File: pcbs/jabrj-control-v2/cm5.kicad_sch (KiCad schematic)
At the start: 26 parts, among them J701 FFC3A20-05-G, J702 JST-SH-4-Vertical, Q701 DMN21D2UFB-7B, SW701 TS20-42-25-WT-160-SMT-TR, U701 PESD4USB3BTTS-QX, U702 NX3DV221GM

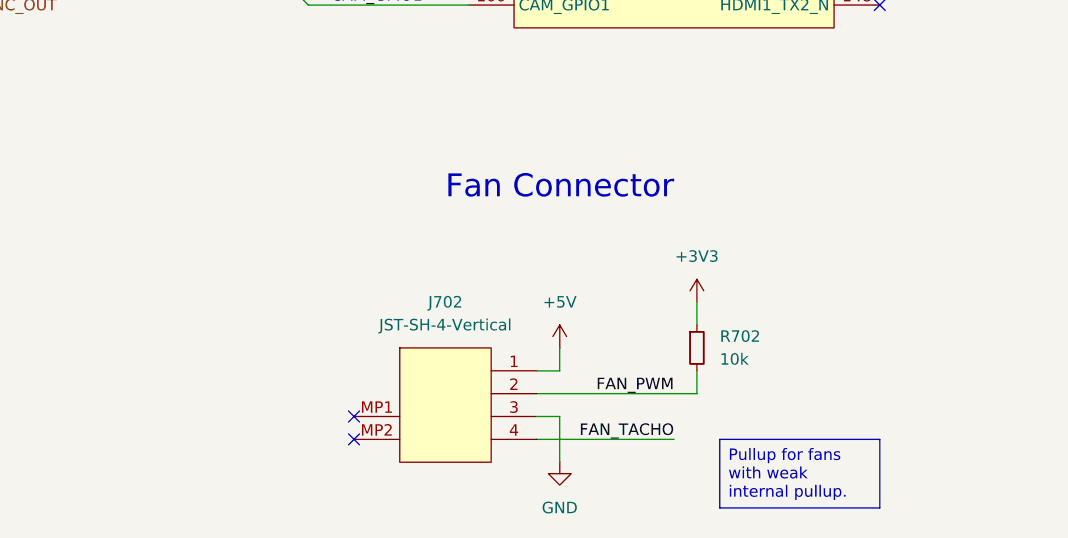
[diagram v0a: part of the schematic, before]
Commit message: Fixed 5V buck inductor value
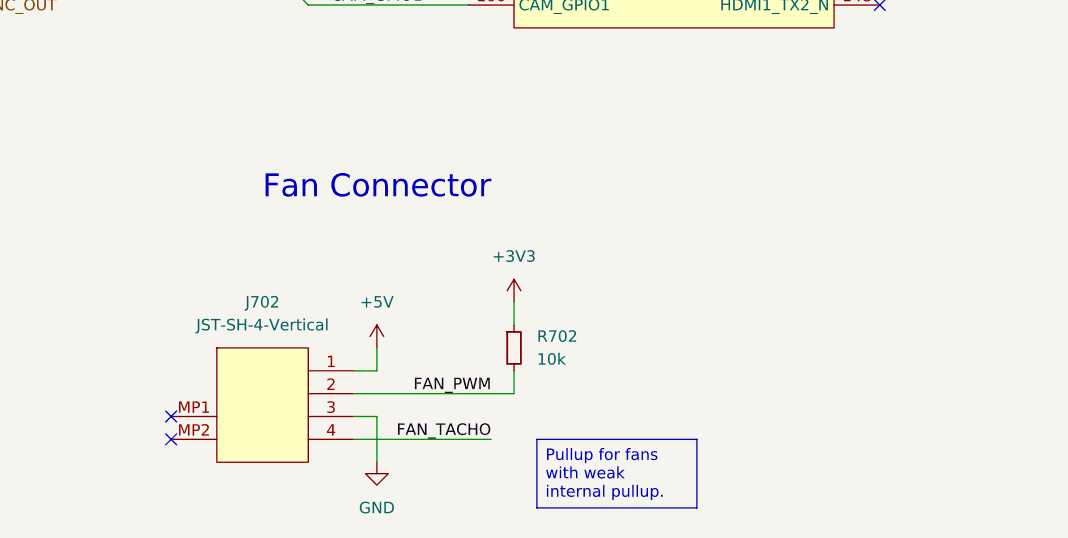
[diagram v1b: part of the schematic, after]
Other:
- moved on the sheet: J702, R702

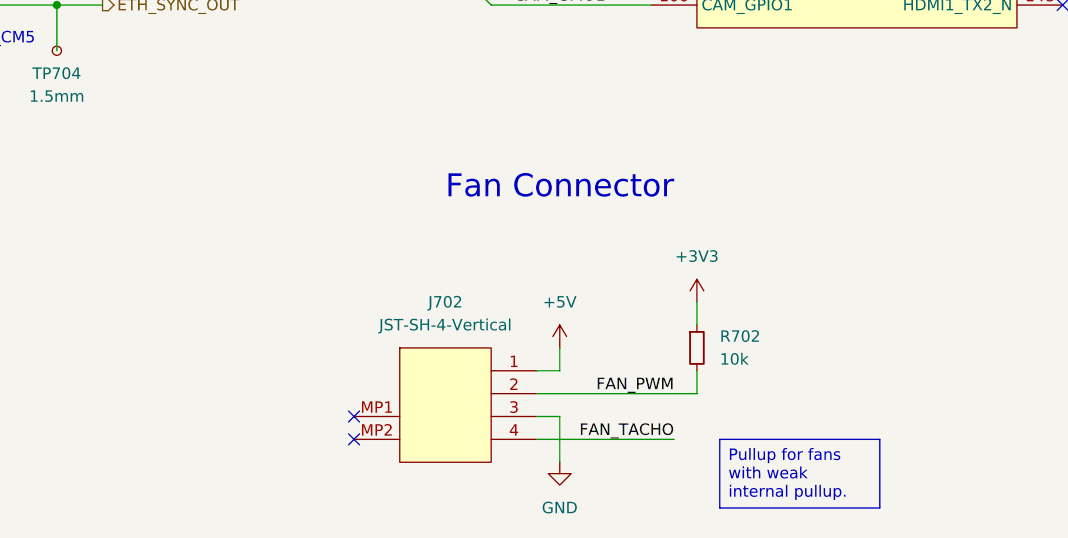
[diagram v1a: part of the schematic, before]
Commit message: Minor schematic fixes
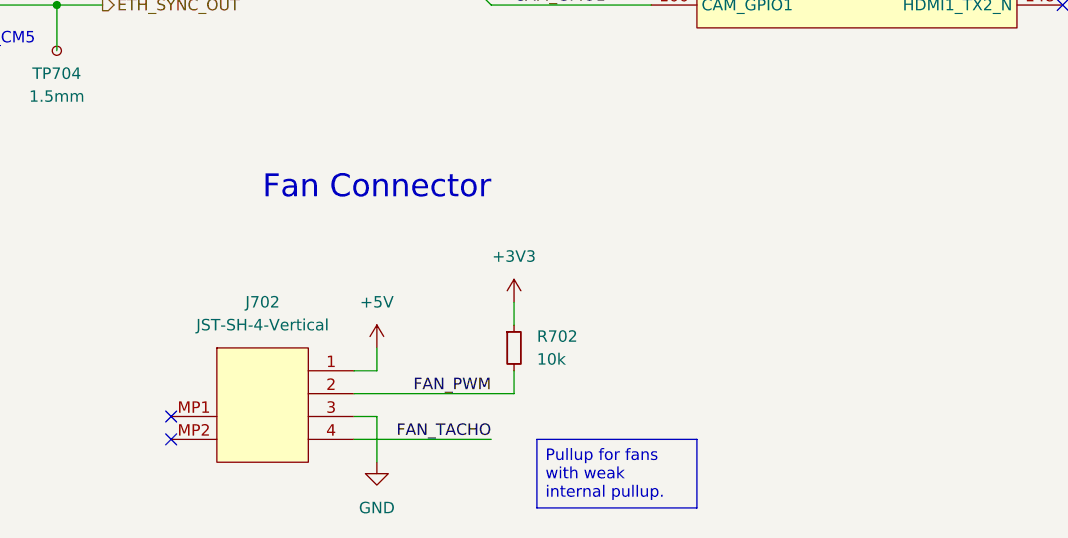
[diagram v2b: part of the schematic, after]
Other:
- moved on the sheet: J702, R702

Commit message: Layout started
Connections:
- net +3V3: now also J701.1
- net +5V: no longer J701.1
- net GND: no longer U702.11 (EP)
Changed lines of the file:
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@@
 	(wire
 		(pts
-			(xy 264.16 78.74) (xy 264.16 81.28)
-		)
-		(stroke
-			(width 0)
-			(type default)
-		)
-	)
-	(wire
-		(pts
 			(xy 228.6 58.42) (xy 231.14 58.42)
 		)
@@
 	(wire
 		(pts
-			(xy 261.62 78.74) (xy 264.16 78.74)
-		)
-		(stroke
-			(width 0)
-			(type default)
-		)
-	)
-	(wire
-		(pts
 			(xy 205.74 208.28) (xy 223.52 208.28)
 		)
@@
 	(wire
 		(pts
+			(xy 43.18 66.04) (xy 43.18 68.58)
+		)
+		(stroke
+			(width 0)
+			(type default)
+		)
+	)
+	(wire
+		(pts
 			(xy 396.24 149.86) (xy 396.24 152.4)
 		)
@@
 	(wire
 		(pts
-			(xy 40.64 68.58) (xy 43.18 68.58)
-		)
-		(stroke
-			(width 0)
-			(type default)
-		)
-	)
-	(wire
-		(pts
 			(xy 347.98 121.92) (xy 345.44 121.92)
 		)
@@
 		)
 	)
-	(wire
-		(pts
-			(xy 43.18 66.04) (xy 43.18 68.58)
-		)
-		(stroke
-			(width 0)
-			(type default)
-		)
-	)
 	(bus
 		(pts
@@
 	(wire
 		(pts
+			(xy 40.64 68.58) (xy 43.18 68.58)
+		)
+		(stroke
+			(width 0)
+			(type default)
+		)
+	)
+	(wire
+		(pts
 			(xy 396.24 190.5) (xy 393.7 190.5)
 		)
@@
 	)
 	(symbol
-		(lib_id "power:+5V")
-		(at 43.18 66.04 0)
-		(unit 1)
-		(body_style 1)
-		(exclude_from_sim no)
-		(in_bom yes)
-		(on_board yes)
-		(in_pos_files yes)
-		(dnp no)
-		(fields_autoplaced yes)
-		(property "Reference" "#PWR0702"
-			(at 43.18 69.85 0)
-			(hide yes)
-			(show_name no)
-			(do_not_autoplace no)
-			(effects
-				(font
-					(size 1.27 1.27)
-				)
-			)
-		)
-		(property "Value" "+5V"
-			(at 43.18 60.96 0)
-			(show_name no)
-			(do_not_autoplace no)
-			(effects
-				(font
-					(size 1.27 1.27)
-				)
-			)
-		)
-		(property "Footprint" ""
-			(at 43.18 66.04 0)
-			(hide yes)
-			(show_name no)
-			(do_not_autoplace no)
-			(effects
-				(font
-					(size 1.27 1.27)
-				)
-			)
-		)
-		(property "Datasheet" ""
-			(at 43.18 66.04 0)
-			(hide yes)
-			(show_name no)
-			(do_not_autoplace no)
-			(effects
-				(font
-					(size 1.27 1.27)
-				)
-			)
-		)
-		(property "Description" "Power symbol creates a global label with name \"+5V\""
-			(at 43.18 66.04 0)
-			(hide yes)
-			(show_name no)
-			(do_not_autoplace no)
-			(effects
-				(font
-					(size 1.27 1.27)
-				)
-			)
-		)
-		(pin "1"
-		)
-		(instances
-			(project "jabrj-control-v2"
-				(path "/f91ec272-d09a-4038-bbbb-962739a92c51/6befb881-6ab4-49eb-a195-35f4f02473c7"
-					(reference "#PWR0702")
-					(unit 1)
-				)
-			)
-		)
-	)
-	(symbol
 		(lib_id "MECH:PCM12SMTBR")
 		(at 320.04 170.18 90)
@@
 		(pin "9"
 		)
-		(pin "11"
-		)
 		(pin "10"
 		)
@@
 	)
 	(symbol
+		(lib_id "power:+3V3")
+		(at 43.18 66.04 0)
+		(unit 1)
+		(body_style 1)
+		(exclude_from_sim no)
+		(in_bom yes)
+		(on_board yes)
+		(in_pos_files yes)
+		(dnp no)
+		(fields_autoplaced yes)
+		(property "Reference" "#PWR0702"
+			(at 43.18 69.85 0)
+			(hide yes)
+			(show_name no)
+			(do_not_autoplace no)
+			(effects
+				(font
+					(size 1.27 1.27)
+				)
+			)
+		)
+		(property "Value" "+3V3"
+			(at 43.18 60.96 0)
+			(show_name no)
+			(do_not_autoplace no)
+			(effects
+				(font
+					(size 1.27 1.27)
+				)
+			)
+		)
+		(property "Footprint" ""
+			(at 43.18 66.04 0)
+			(hide yes)
+			(show_name no)
+			(do_not_autoplace no)
+			(effects
+				(font
+					(size 1.27 1.27)
+				)
+			)
+		)
+		(property "Datasheet" ""
+			(at 43.18 66.04 0)
+			(hide yes)
+			(show_name no)
+			(do_not_autoplace no)
+			(effects
+				(font
+					(size 1.27 1.27)
+				)
+			)
+		)
+		(property "Description" "Power symbol creates a global label with name \"+3V3\""
+			(at 43.18 66.04 0)
+			(hide yes)
+			(show_name no)
+			(do_not_autoplace no)
+			(effects
+				(font
+					(size 1.27 1.27)
+				)
+			)
+		)
+		(pin "1"
+		)
+		(instances
+			(project "jabrj-control-v2"
+				(path "/f91ec272-d09a-4038-bbbb-962739a92c51/6befb881-6ab4-49eb-a195-35f4f02473c7"
+					(reference "#PWR0702")
+					(unit 1)
+				)
+			)
+		)
+	)
+	(symbol
 		(lib_id "power:GND")
 		(at 396.24 213.36 0)
@@
 					(unit 1)
 				)
-			)
-		)
-	)
-	(symbol
-		(lib_id "power:GND")
-		(at 264.16 81.28 0)
-		(unit 1)
-		(body_style 1)
-		(exclude_from_sim no)
-		(in_bom yes)
-		(on_board yes)
-		(in_pos_files yes)
-		(dnp no)
-		(fields_autoplaced yes)
-		(property "Reference" "#PWR0714"
-			(at 264.16 87.63 0)
-			(hide yes)
-			(show_name no)
-			(do_not_autoplace no)
-			(effects
-				(font
-					(size 1.27 1.27)
-				)
-			)
-		)
-		(property "Value" "GND"
-			(at 264.16 86.36 0)
-			(show_name no)
-			(do_not_autoplace no)
-			(effects
-				(font
-					(size 1.27 1.27)
-				)
-			)
-		)
-		(property "Footprint" ""
-			(at 264.16 81.28 0)
-			(hide yes)
-			(show_name no)
-			(do_not_autoplace no)
-			(effects
-				(font
-					(size 1.27 1.27)
-				)
-			)
-		)
-		(property "Datasheet" ""
-			(at 264.16 81.28 0)
-			(hide yes)
-			(show_name no)
-			(do_not_autoplace no)
-			(effects
-				(font
-					(size 1.27 1.27)
-				)
-			)
-		)
-		(property "Description" "Power symbol creates a global label with name \"GND\" , ground"
-			(at 264.16 81.28 0)
-			(hide yes)
-			(show_name no)
-			(do_not_autoplace no)
-			(effects
-				(font
-					(size 1.27 1.27)
-				)
-			)
-		)
-		(pin "1"
-		)
-		(instances
-			(project "jabrj-control-v2"
-				(path "/f91ec272-d09a-4038-bbbb-962739a92c51/6befb881-6ab4-49eb-a195-35f4f02473c7"
-					(reference "#PWR0714")
-					(unit 1)
-				)

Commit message: Layout almost done
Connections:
- net DN: no longer TP703.1
- net DP: no longer TP702.1
- net USB2_DEV.DN: now also TP703.1
- net USB2_DEV.DP: now also TP702.1

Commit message: 895 Unrouted
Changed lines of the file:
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@@
 		)
 	)
+	(text_box "CM5 PCIe can be either gen 2 (100Ω) or gen 3 (85Ω) so route at 90Ω as recommended by Raspberry Pi."
+		(exclude_from_sim no)
+		(at 40.64 195.58 0)
+		(size 27.94 12.7)
+		(margins 0.9525 0.9525 0.9525 0.9525)
+		(stroke
+			(width 0)
+			(type solid)
+		)
+		(fill
+			(type none)
+		)
+		(effects
+			(font
+				(size 1.27 1.27)
+			)
+			(justify left top)
+		)
+	)
 	(text_box "Pullup for fans with weak internal pullup."
 		(exclude_from_sim no)
@@
 		(length 2.54)
 		(shape round)
-		(at 73.66 190.5 0)
+		(at 203.2 157.48 0)
 		(fields_autoplaced yes)
 		(effects
@@
 			(justify left bottom)
 		)
-		(property "Net Class" "PCIe"
-			(at 74.3585 187.96 0)
+		(property "Net Class" "MIPI"
+			(at 203.8985 154.94 0)
 			(show_name no)
 			(do_not_autoplace no)
@@
 		)
 		(property "Component Class" ""
-			(at 27.94 83.82 0)
+			(at -73.66 60.96 0)
 			(show_name no)
 			(do_not_autoplace no)
@@
 		(length 2.54)
 		(shape round)
+		(at 73.66 190.5 0)
+		(fields_autoplaced yes)
+		(effects
+			(font
+				(size 1.27 1.27)
+			)
+			(justify left bottom)
+		)
+		(property "Net Class" "PCIe (90Ω)"
+			(at 74.3585 187.96 0)
+			(show_name no)
+			(do_not_autoplace no)
+			(effects
+				(font
+					(size 1.27 1.27)
+				)
+				(justify left)
+			)
+		)
+		(property "Component Class" ""
+			(at -86.36 91.44 0)
+			(show_name no)
+			(do_not_autoplace no)
+			(effects
+				(font
+					(size 1.27 1.27)
+					(italic yes)
+				)
+			)
+		)
+	)
+	(netclass_flag ""
+		(length 2.54)
+		(shape round)
 		(at 175.26 60.96 0)
 		(fields_autoplaced yes)
@@
 			(show_name no)
 			(do_not_autoplace no)
+			(effects
+				(font
+					(size 1.27 1.27)
+					(italic yes)
+				)
+			)
+		)
+	)
+	(netclass_flag ""
+		(length 2.54)
+		(shape round)
+		(at 203.2 116.84 0)
+		(fields_autoplaced yes)
+		(effects
+			(font
+				(size 1.27 1.27)
+			)
+			(justify left bottom)
+		)
+		(property "Net Class" "MIPI"
+			(at 203.8985 114.3 0)
+			(show_name no)
+			(do_not_autoplace no)
+			(effects
+				(font
+					(size 1.27 1.27)
+				)
+				(justify left)
+			)
+		)
+		(property "Component Class" ""
+			(at -73.66 20.32 0)
+			(show_name no)
+			(do_not_autoplace no)

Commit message: 651 Unrouted
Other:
- moved on the sheet: D704, D705, TP702, TP703, TP705

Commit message: 603 Unrouted
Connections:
- net CAM_GPIO2: now also SOM701.58 (GPIO2)
- net I2C3.INT: now reaches SOM701.45 (GPIO24)
- net I2C3.SDA: now reaches SOM701.46 (GPIO22)
- net I2C3.SCL: now reaches SOM701.47 (GPIO23)
- no-connect marks 66 -> 62
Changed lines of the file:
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@@
 	(text_box "GPIO27 Connects to the PCI11010C's PTP_IO6. PTP_IO6 can be configured to be a PPS output and GPIO27 as a PPS input."
 		(exclude_from_sim no)
-		(at 48.26 116.84 0)
+		(at 22.86 127 0)
 		(size 38.1 10.16)
 		(margins 0.9525 0.9525 0.9525 0.9525)
@@
 	)
 	(no_connect
-		(at 93.98 124.46)
-	)
-	(no_connect
 		(at 170.18 256.54)
 	)
@@
 	)
 	(no_connect
-		(at 93.98 121.92)
-	)
-	(no_connect
 		(at 93.98 116.84)
 	)
@@
 	)
 	(no_connect
-		(at 93.98 68.58)
-	)
-	(no_connect
 		(at 93.98 91.44)
 	)
@@
 	)
 	(no_connect
-		(at 93.98 119.38)
-	)
-	(no_connect
 		(at 347.98 167.64)
 	)
@@
 	)
 	(bus_entry
+		(at 76.2 116.84)
+		(size 2.54 2.54)
+		(stroke
+			(width 0)
+			(type default)
+		)
+	)
+	(bus_entry
 		(at 203.2 157.48)
 		(size 2.54 2.54)
@@
 	)
 	(bus_entry
+		(at 76.2 121.92)
+		(size 2.54 2.54)
+		(stroke
+			(width 0)
+			(type default)
+		)
+	)
+	(bus_entry
 		(at 160.02 93.98)
 		(size -2.54 2.54)
@@
 	)
 	(bus_entry
+		(at 76.2 119.38)
+		(size 2.54 2.54)
+		(stroke
+			(width 0)
+			(type default)
+		)
+	)
+	(bus_entry
 		(at 91.44 254)
 		(size 2.54 2.54)
@@
 	(wire
 		(pts
-			(xy 71.12 106.68) (xy 86.36 106.68)
+			(xy 81.28 68.58) (xy 93.98 68.58)
 		)
 		(stroke
@@
 		)
 	)
+	(bus
+		(pts
+			(xy 76.2 119.38) (xy 76.2 121.92)
+		)
+		(stroke
+			(width 0)
+			(type default)
+		)
+	)
 	(wire
 		(pts
@@
 	(wire
 		(pts
+			(xy 78.74 124.46) (xy 93.98 124.46)
+		)
+		(stroke
+			(width 0)
+			(type default)
+		)
+	)
+	(wire
+		(pts
 			(xy 205.74 190.5) (xy 223.52 190.5)
 		)
@@
 	(wire
 		(pts
+			(xy 78.74 119.38) (xy 93.98 119.38)
+		)
+		(stroke
+			(width 0)
+			(type default)
+		)
+	)
+	(wire
+		(pts
 			(xy 396.24 162.56) (xy 393.7 162.56)
 		)
@@
 		)
 	)
+	(wire
+		(pts
+			(xy 78.74 121.92) (xy 93.98 121.92)
+		)
+		(stroke
+			(width 0)
+			(type default)
+		)
+	)
 	(bus
 		(pts
@@
 		)
 	)
+	(bus
+		(pts
+			(xy 73.66 116.84) (xy 76.2 116.84)
+		)
+		(stroke
+			(width 0)
+			(type default)
+		)
+	)
 	(wire
 		(pts
@@
 		)
 	)
+	(bus
+		(pts
+			(xy 76.2 116.84) (xy 76.2 119.38)
+		)
+		(stroke
+			(width 0)
+			(type default)
+		)
+	)
 	(wire
 		(pts
@@
 	)
 	(label "CAM_GPIO2"
-		(at 71.12 106.68 0)
+		(at 81.28 68.58 0)
 		(effects
 			(font
@@
 		)
 	)
+	(label "I2C3.SDA"
+		(at 81.28 119.38 0)
+		(effects
+			(font
+				(size 1.27 1.27)
+			)
+			(justify left bottom)
+		)
+	)
 	(label "CAM_GPIO1"
 		(at 109.22 254 180)
@@
 		)
 	)
+	(label "I2C3.INT"
+		(at 81.28 124.46 0)
+		(effects
+			(font
+				(size 1.27 1.27)
+			)
+			(justify left bottom)
+		)
+	)
 	(label "MIPI1.D1_N"
 		(at 208.28 177.8 0)
@@
 		)
 	)
+	(label "I2C3.SCL"
+		(at 81.28 121.92 0)
+		(effects
+			(font
+				(size 1.27 1.27)
+			)
+			(justify left bottom)
+		)
+	)
 	(label "MIPI0.D0_N"
 		(at 208.28 129.54 0)
@@
 		)
 	)
+	(hierarchical_label "I2C3{I2C}"
+		(shape bidirectional)
+		(at 73.66 116.84 180)
+		(effects
+			(font
+				(size 1.27 1.27)
+			)
+			(justify right)
+		)
+	)
 	(hierarchical_label "I2C2{I2C}"
 		(shape bidirectional)
@@
 		)
 	)
-	(hierarchical_label "CAM_GPIO[0..1]"
+	(hierarchical_label "CAM_GPIO[0..2]"
 		(shape bidirectional)
 		(at 88.9 248.92 180)

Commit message: 400 Unrouted
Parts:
- removed J701: FFC3A20-05-G, project_footprints:FFC3A2005G, symbol CONN-FPC:FFC3A20-05-G
- removed U701: PESD4USB3BTTS-QX, project_footprints:PESD4USB3BTTSQX, symbol TVS:PESD4USB3BTTS-QX
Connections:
- net I2C3.INT renamed I2C3.~{INT}
- net NRST_CONN renamed UART2.~{RST}
- net RX renamed UART2.RX
- net TX renamed UART2.TX
- no-connect marks 62 -> 61
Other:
- moved on the sheet: D701
